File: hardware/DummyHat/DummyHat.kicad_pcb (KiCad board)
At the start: 2 copper layers, 38.1 x 73.8 mm, 41 parts, among them J1 Conn_01x08_Socket, J2 Conn_01x08_Socket, J3 Conn_01x08_Socket, Q1 PZT2222A, U1 74HC688, U2 74HC245, U3 74HC245

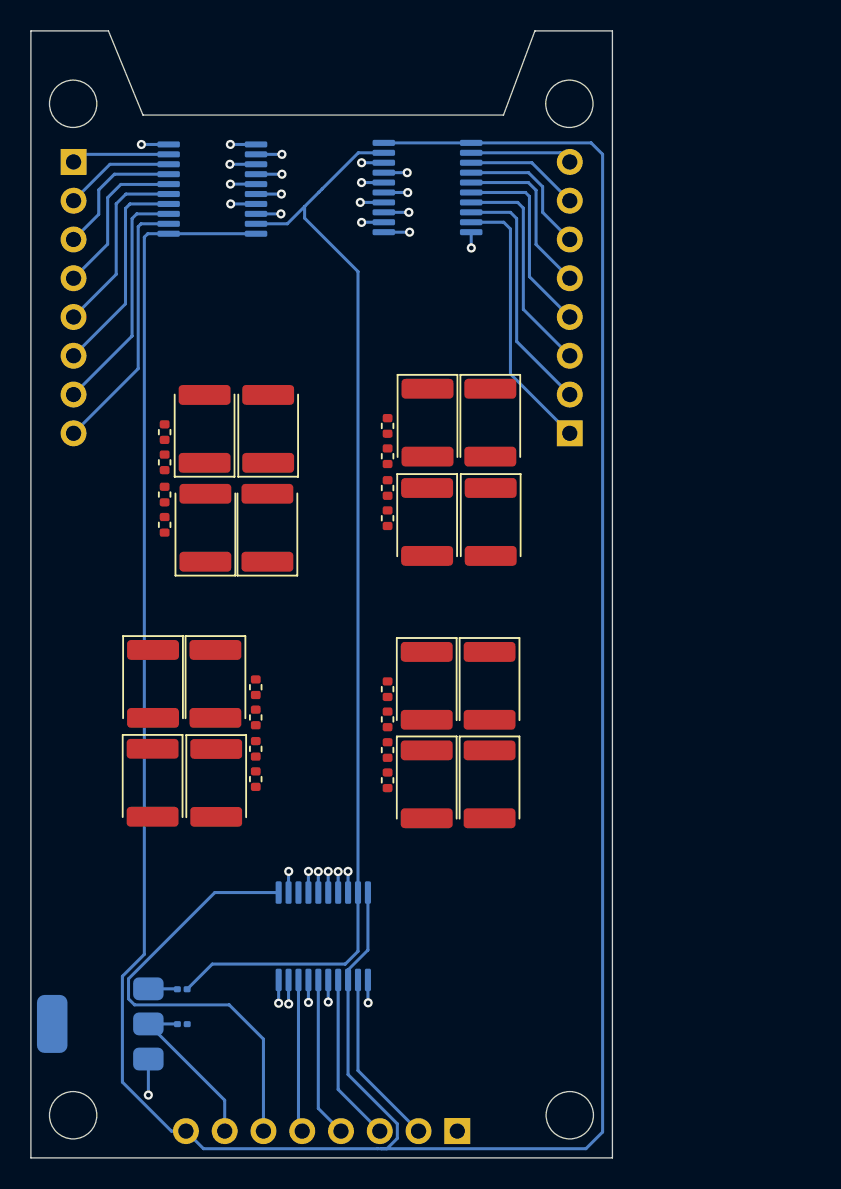
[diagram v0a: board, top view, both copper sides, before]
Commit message: changed voltage selector to actually work
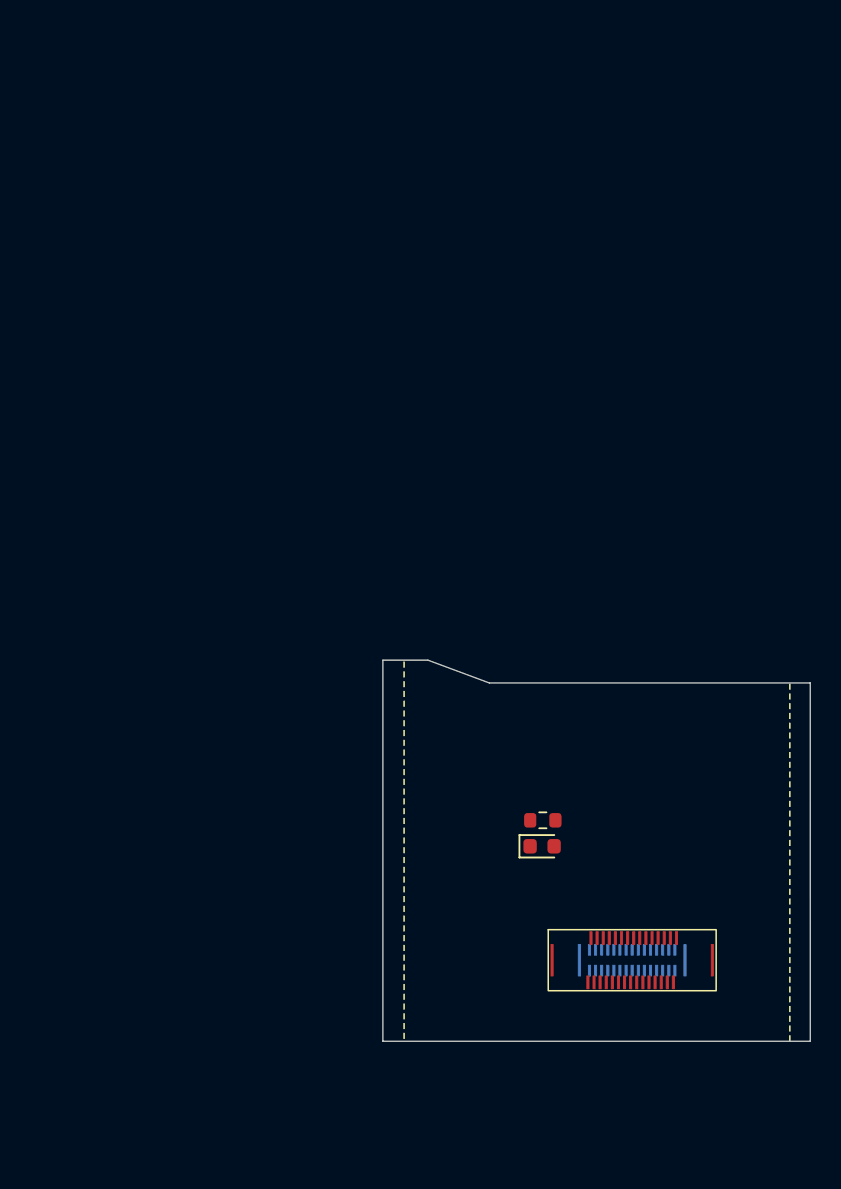
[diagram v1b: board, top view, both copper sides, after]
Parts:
- removed D10, D11, D12, D13, D14, D15, D16, D2, D3, D4, D5, D6, D7, D8, D9: LED, LED_SMD:LED_1812_4532Metric_Pad1.30x3.40mm_HandSolder
- removed J3: Conn_01x08_Socket, Connector_PinSocket_2.54mm:PinSocket_1x08_P2.54mm_Vertical
- removed Q1: PZT2222A, Package_TO_SOT_SMD:SOT-223-3_TabPin2
- removed R10, R11, R12, R13, R14, R15, R16, R17, R18, R3, R4, R5, R6, R7, R8, R9: R, Resistor_SMD:R_0402_1005Metric
- removed R2: 1k, Resistor_SMD:R_0201_0603Metric
- removed U1: 74HC688, Package_SO:TSSOP-20_4.4x6.5mm_P0.65mm
- removed U2, U3: 74HC245, Package_SO:TSSOP-20_4.4x6.5mm_P0.65mm
- D1: footprint LED_SMD:LED_1812_4532Metric_Pad1.30x3.40mm_HandSolder -> LED_SMD:LED_0603_1608Metric
- J1: value Conn_01x08_Socket -> Conn_02x16_Top_Bottom; footprint Connector_PinSocket_2.54mm:PinSocket_1x08_P2.54mm_Vertical -> MolexFSB:FSB5 Series 0.40 mm Pitch Floating SlimStack Board-to-Board Receptacles
- J2: value Conn_01x08_Socket -> Conn_02x16_Top_Bottom; footprint Connector_PinSocket_2.54mm:PinSocket_1x08_P2.54mm_Vertical -> MolexFSB:FSB5 Series 0.40 mm Pitch Floating SlimStack Board-to-Board Plugs; moved to F.Cu
- R1: value 1k -> R; footprint Resistor_SMD:R_0201_0603Metric -> Resistor_SMD:R_0603_1608Metric; moved to F.Cu
- moved J2 63.8 mm to (90.2, 109.7), turned to 0 degrees
- moved D1 27.6 mm to (84.3, 102.2), turned to 0 degrees
- moved R1 26.1 mm to (84.3, 100.5), turned to 0 degrees
- moved J1 16.0 mm to (90.2, 109.7), turned to 0 degrees
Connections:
- D1 pad 2: D5 -> CONN_0
- J1 pad 1: GND -> CONN_0
- J1 pad 2: I0 -> CONN_1
- J1 pad 3: I1 -> CONN_2
- J1 pad 4: I2 -> CONN_3
- J1 pad 5: I3 -> CONN_4
- J1 pad 6: I4 -> CONN_5
- J1 pad 7: RESP -> CONN_6
- J1 pad 8: +5V -> CONN_7
- J2 pad 1: Net-(J2-Pin_1) -> CONN_15
- J2 pad 2: Net-(J2-Pin_2) -> CONN_16
- J2 pad 3: Net-(J2-Pin_3) -> CONN_17
- J2 pad 4: Net-(J2-Pin_4) -> CONN_18
- J2 pad 5: Net-(J2-Pin_5) -> CONN_19
- J2 pad 6: Net-(J2-Pin_6) -> CONN_20
- J2 pad 7: Net-(J2-Pin_7) -> CONN_21
- J2 pad 8: Net-(J2-Pin_8) -> CONN_22
- R1 pad 1: Net-(U1-P=R) -> GND
- R1 pad 2: Net-(Q1-B) -> Net-(D1-K)
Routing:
- net +5V: track 195.1 -> 0.00 mm
- net Net-(U1-P=R): track 72.8 -> 0.00 mm
- net I4: track 29.4 -> 0.00 mm
- net GND: track 21.1 -> 0.00 mm, vias 14 -> 0
- net Net-(J3-Pin_1): track 17.8 -> 0.00 mm
- net Net-(J2-Pin_8): track 17.4 -> 0.00 mm
- net Net-(J3-Pin_2): track 16.1 -> 0.00 mm
- net Net-(J2-Pin_7): track 15.6 -> 0.00 mm
- net Net-(J3-Pin_3): track 14.5 -> 0.00 mm
- net Net-(J2-Pin_6): track 14.0 -> 0.00 mm
- net Net-(J3-Pin_4): track 12.9 -> 0.00 mm
- net Net-(J2-Pin_5): track 12.3 -> 0.00 mm
- net I0: track 11.5 -> 0.00 mm
- net Net-(J3-Pin_5): track 11.1 -> 0.00 mm
- net I1: track 11.0 -> 0.00 mm
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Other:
- board size 38.1 x 73.8 mm -> 28 x 25 mm
